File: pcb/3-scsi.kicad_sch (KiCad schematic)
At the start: 0 parts

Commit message: Phase 3: populate SCSI sheet and channel sheets
SCSI sheet (A2): IDC50 and HD50 wired by signal name from SCSI-2
Table 2, all four RESERVED lines grounded through 0R links, the
logic-analyzer header as a pin-for-pin copy of the Digital Discovery
DIN connector, three SN74LVTH245A terminators with their DIP-switch
enable and truth table, and one cluster per line: 2 x 220R terminator
pair, ESD diode and channel sheet. Channel sheets hold the FDV301N
driver and the 74LVC1G17 receiver; 18 instances, references page x 100.

Generator: repeated sheets, sheet symbols, native tables, and
deterministic UUIDs. Nets renamed: LA -> LOGIC_ANALYZER,
TERMINATOR_EN -> TERMINATOR_EN_INVERTED_FIRMWARE.
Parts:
- added C301, C302, C303: 100nF 50V, Capacitor_SMD:C_0402_1005Metric, symbol Device:C
- added D301, D302, D303, D304, D305, D306, D307, D308, D309, D310, D311, D312, D313, D314, D315, D316, D317, D318: H5VUD5BB, Diode_SMD:D_SOD-523, symbol Device:D_TVS
- added J301: IDC50 box header, Connector_IDC:IDC-Header_2x25_P2.54mm_Vertical, symbol Connector_Generic:Conn_02x25_Odd_Even
- added J302: HD50 female R/A, symbol Connector_Generic:Conn_02x25_Top_Bottom
- added J303: 2x16 box header, Connector_IDC:IDC-Header_2x16_P2.54mm_Vertical, symbol Connector_Generic:Conn_02x16_Odd_Even
- added R301, R302, R303, R304, R305, R306, R307, R308, R309, R310, R311, R312, R313, R314, R315, R316, R317, R318, R319, R320, R321, R322, R323, R324, R325, R326, R327, R328, R329, R330, R331, R332, R333, R334, R335, R336: 220R, Resistor_SMD:R_0402_1005Metric, symbol Device:R
- added R337, R338, R339, R340: 0R, Resistor_SMD:R_0402_1005Metric, symbol Device:R
- added R341: 10k, Resistor_SMD:R_0402_1005Metric, symbol Device:R
- added R342: 1k, Resistor_SMD:R_0402_1005Metric, symbol Device:R
- added SW301: DIP 2-pos, symbol Switch:SW_DIP_x02
- added U301, U302, U303: SN74LVTH245APWR, Package_SO:TSSOP-20_4.4x6.5mm_P0.65mm, symbol scsi-adapter:SN74LVTH245A
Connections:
- net ~{ACK}: now also D312.1 (A1), J301.38 (Pin_38), J302.44 (Pin_44), R323.2, R324.2
- net ~{ATN}: now also D310.1 (A1), J301.32 (Pin_32), J302.41 (Pin_41), R319.2, R320.2
- net ~{BSY}: now also D311.1 (A1), J301.36 (Pin_36), J302.43 (Pin_43), R321.2, R322.2
- net ~{CD}: now also D316.1 (A1), J301.46 (Pin_46), J302.48 (Pin_48), R331.2, R332.2
- net ~{DB0}: now also D301.1 (A1), J301.2 (Pin_2), J302.26 (Pin_26), R301.2, R302.2
- net ~{DB1}: now also D302.1 (A1), J301.4 (Pin_4), J302.27 (Pin_27), R303.2, R304.2
- net ~{DB2}: now also D303.1 (A1), J301.6 (Pin_6), J302.28 (Pin_28), R305.2, R306.2
- net ~{DB3}: now also D304.1 (A1), J301.8 (Pin_8), J302.29 (Pin_29), R307.2, R308.2
- net ~{DB4}: now also D305.1 (A1), J301.10 (Pin_10), J302.30 (Pin_30), R309.2, R310.2
- net ~{DB5}: now also D306.1 (A1), J301.12 (Pin_12), J302.31 (Pin_31), R311.2, R312.2
- net ~{DB6}: now also D307.1 (A1), J301.14 (Pin_14), J302.32 (Pin_32), R313.2, R314.2
- net ~{DB7}: now also D308.1 (A1), J301.16 (Pin_16), J302.33 (Pin_33), R315.2, R316.2
- net ~{DBP}: now also D309.1 (A1), J301.18 (Pin_18), J302.34 (Pin_34), R317.2, R318.2
- net ~{IO}: now also D318.1 (A1), J301.50 (Pin_50), J302.50 (Pin_50), R335.2, R336.2
- net ~{MSG}: now also D314.1 (A1), J301.42 (Pin_42), J302.46 (Pin_46), R327.2, R328.2
- net ~{REQ}: now also D317.1 (A1), J301.48 (Pin_48), J302.49 (Pin_49), R333.2, R334.2
- net ~{RST}: now also D313.1 (A1), J301.40 (Pin_40), J302.45 (Pin_45), R325.2, R326.2
- net ~{SEL}: now also D315.1 (A1), J301.44 (Pin_44), J302.47 (Pin_47), R329.2, R330.2
- new net: R342.1, SW301.4
- new net ACK_LOGIC_ANALYZER: J303.13 (Pin_13)
- new net ATN_LOGIC_ANALYZER: J303.17 (Pin_17)
- new net BSY_LOGIC_ANALYZER: J303.15 (Pin_15)
- new net CD_LOGIC_ANALYZER: J303.14 (Pin_14)
- new net DB0_LOGIC_ANALYZER: J303.29 (Pin_29)
- new net DB1_LOGIC_ANALYZER: J303.27 (Pin_27)
- new net DB2_LOGIC_ANALYZER: J303.25 (Pin_25)
- new net DB3_LOGIC_ANALYZER: J303.23 (Pin_23)
- new net DB4_LOGIC_ANALYZER: J303.30 (Pin_30)
- new net DB5_LOGIC_ANALYZER: J303.28 (Pin_28)
- new net DB6_LOGIC_ANALYZER: J303.26 (Pin_26)
- new net DB7_LOGIC_ANALYZER: J303.24 (Pin_24)
- new net DBP_LOGIC_ANALYZER: J303.19 (Pin_19)
- new net GND: C301.2, C302.2, C303.2, D301.2 (A2), D302.2 (A2), D303.2 (A2), D304.2 (A2), D305.2 (A2), D306.2 (A2), D307.2 (A2), D308.2 (A2), D309.2 (A2), D310.2 (A2), D311.2 (A2), D312.2 (A2), D313.2 (A2), D314.2 (A2), D315.2 (A2), D316.2 (A2), D317.2 (A2), D318.2 (A2), J301.1 (Pin_1), J301.11 (Pin_11), J301.13 (Pin_13), J301.15 (Pin_15), J301.17 (Pin_17), J301.19 (Pin_19), J301.20 (Pin_20), J301.21 (Pin_21), J301.22 (Pin_22), J301.29 (Pin_29), J301.3 (Pin_3), J301.30 (Pin_30), J301.31 (Pin_31), J301.33 (Pin_33), J301.34 (Pin_34), J301.35 (Pin_35), J301.37 (Pin_37), J301.39 (Pin_39), J301.41 (Pin_41), J301.43 (Pin_43), J301.45 (Pin_45), J301.47 (Pin_47), J301.49 (Pin_49), J301.5 (Pin_5), J301.7 (Pin_7), J301.9 (Pin_9), J302.1 (Pin_1), J302.10 (Pin_10), J302.11 (Pin_11), J302.15 (Pin_15), J302.16 (Pin_16), J302.17 (Pin_17), J302.18 (Pin_18), J302.19 (Pin_19), J302.2 (Pin_2), J302.20 (Pin_20), J302.21 (Pin_21), J302.22 (Pin_22), J302.23 (Pin_23), J302.24 (Pin_24), J302.25 (Pin_25), J302.3 (Pin_3), J302.35 (Pin_35), J302.36 (Pin_36), J302.4 (Pin_4), J302.40 (Pin_40), J302.42 (Pin_42), J302.5 (Pin_5), J302.6 (Pin_6), J302.7 (Pin_7), J302.8 (Pin_8), J302.9 (Pin_9), J303.1 (Pin_1), J303.11 (Pin_11), J303.12 (Pin_12), J303.2 (Pin_2), J303.21 (Pin_21), J303.22 (Pin_22), J303.31 (Pin_31), J303.32 (Pin_32), R337.2, R338.2, R339.2, R340.2, R342.2, U301.10 (GND), U302.10 (GND), U303.10 (GND)
- new net IO_LOGIC_ANALYZER: J303.7 (Pin_7)
- new net LOGIC_ANALYZER_MARKER0: J303.5 (Pin_5)
- new net LOGIC_ANALYZER_MARKER1: J303.3 (Pin_3)
- new net MSG_LOGIC_ANALYZER: J303.18 (Pin_18)
- new net REQ_LOGIC_ANALYZER: J303.9 (Pin_9)
- new net RST_LOGIC_ANALYZER: J303.20 (Pin_20)
- new net SCSI_RESERVED_23: J301.23 (Pin_23), J302.12 (Pin_12), R337.1
- new net SCSI_RESERVED_24: J301.24 (Pin_24), J302.37 (Pin_37), R338.1
- new net SCSI_RESERVED_27: J301.27 (Pin_27), J302.14 (Pin_14), R339.1
- new net SCSI_RESERVED_28: J301.28 (Pin_28), J302.39 (Pin_39), R340.1
- new net SEL_LOGIC_ANALYZER: J303.16 (Pin_16)
- new net TERMINATOR_EN_INVERTED: R341.2, SW301.1, SW301.2, U301.19 (CE), U302.19 (CE), U303.19 (CE)
- new net TERMINATOR_EN_INVERTED_FIRMWARE: SW301.3
- new net TERMINATOR_OUT_ACK: R323.1, R324.1, U302.13 (B5)
- new net TERMINATOR_OUT_ATN: R319.1, R320.1, U302.15 (B3)
- new net TERMINATOR_OUT_BSY: R321.1, R322.1, U302.14 (B4)
- new net TERMINATOR_OUT_CD: R331.1, R332.1, U303.15 (B3)
- new net TERMINATOR_OUT_DB0: R301.1, R302.1, U301.18 (B0)
- new net TERMINATOR_OUT_DB1: R303.1, R304.1, U301.17 (B1)
- new net TERMINATOR_OUT_DB2: R305.1, R306.1, U301.16 (B2)
- new net TERMINATOR_OUT_DB3: R307.1, R308.1, U301.15 (B3)
- new net TERMINATOR_OUT_DB4: R309.1, R310.1, U301.14 (B4)
- new net TERMINATOR_OUT_DB5: R311.1, R312.1, U301.13 (B5)
- new net TERMINATOR_OUT_DB6: R313.1, R314.1, U302.18 (B0)
- new net TERMINATOR_OUT_DB7: R315.1, R316.1, U302.17 (B1)
- new net TERMINATOR_OUT_DBP: R317.1, R318.1, U302.16 (B2)
- new net TERMINATOR_OUT_IO: R335.1, R336.1, U303.13 (B5)
- new net TERMINATOR_OUT_MSG: R327.1, R328.1, U303.17 (B1)
- new net TERMINATOR_OUT_REQ: R333.1, R334.1, U303.14 (B4)
- new net TERMINATOR_OUT_RST: R325.1, R326.1, U303.18 (B0)
- new net TERMINATOR_OUT_SEL: R329.1, R330.1, U303.16 (B2)
- new net TERMPWR: J301.26 (Pin_26), J302.38 (Pin_38)
- new net VTERMINATOR: C301.1, C302.1, C303.1, R341.1, U301.1 (A->B), U301.2 (A0), U301.20 (VCC), U301.3 (A1), U301.4 (A2), U301.5 (A3), U301.6 (A4), U301.7 (A5), U301.8 (A6), U301.9 (A7), U302.1 (A->B), U302.2 (A0), U302.20 (VCC), U302.3 (A1), U302.4 (A2), U302.5 (A3), U302.6 (A4), U302.7 (A5), U302.8 (A6), U302.9 (A7), U303.1 (A->B), U303.2 (A0), U303.20 (VCC), U303.3 (A1), U303.4 (A2), U303.5 (A3), U303.6 (A4), U303.7 (A5), U303.8 (A6), U303.9 (A7)
- no-connect marks 0 -> 12
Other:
- sheet ACK ports: added LOGIC_ANALYZER; removed LA
- sheet ATN ports: added LOGIC_ANALYZER; removed LA
- sheet BSY ports: added LOGIC_ANALYZER; removed LA
- sheet CD ports: added LOGIC_ANALYZER; removed LA
- sheet DB0 ports: added LOGIC_ANALYZER; removed LA
- sheet DB1 ports: added LOGIC_ANALYZER; removed LA
- sheet DB2 ports: added LOGIC_ANALYZER; removed LA
- sheet DB3 ports: added LOGIC_ANALYZER; removed LA
- sheet DB4 ports: added LOGIC_ANALYZER; removed LA
- sheet DB5 ports: added LOGIC_ANALYZER; removed LA
- sheet DB6 ports: added LOGIC_ANALYZER; removed LA
- sheet DB7 ports: added LOGIC_ANALYZER; removed LA
- sheet DBP ports: added LOGIC_ANALYZER; removed LA
- sheet IO ports: added LOGIC_ANALYZER; removed LA
- sheet MSG ports: added LOGIC_ANALYZER; removed LA
- sheet REQ ports: added LOGIC_ANALYZER; removed LA
- sheet RST ports: added LOGIC_ANALYZER; removed LA
- sheet SEL ports: added LOGIC_ANALYZER; removed LA
- note added: "A1-A8 and DIR tie straight to the rail: DIR high = A->B, and bus-hold inputs mustn't get pull resistors. B7/B8 unused."
- note added: "Active terminator"
- note added: "Connectors"
- note added: "J301 SCSI IDC50 (fitted)"
- note added: "J302 SCSI HD50 (DNP)"
- note added: "J303 logic-analyzer header (Digital Discovery DIN)"
- note added: "MSG, C/D, REQ, I/O: only the target drives them (SCSI-2 Table 6), so no driver."
- note added: "Per line: terminator pair (2 x 220R = 110R), ESD diode to GND, then the channel sheet (driver + receiver). Keep each cluster on its own bus trace by the connector. GATE (from the RP2350) and RX (to it) are sheet pins."
- note added: "Per-line driver and receiver"
- note added: "Pin 25 (HD50 13) is OPEN: a reversed ribbon puts TERMPWR on a dead pin, not on ground. IDC50 even pins 20, 22, 30, 34 are GROUND."
- note added: "Pin-for-pin copy of the Digital Discovery's 2x16 DIN connector (reference manual Fig. 8): a straight 32-way 0.1" IDC ribbon links pin n to pin n. DIN0-17 = the 18 bus lines in GPIO order (DB0..IO), DIN18/19 = the two markers, DIN20-23 unused. GND on 1, 2, 11, 12, 21, 22, 31, 32. Each tap has 100R at its receiver (channel sheets)."
- note added: "R301-R336: 220R 1 % 0402 (C25091), <= 35 mW each at 2.94 V into an asserted line. D301-D318: H5VUD5BB (C20615820), bidirectional, 0.3 pF, 5 V working. ESD protection: they clamp static discharges from the cable or a finger on the connector to GND before they reach the FET or the receiver. 0.3 pF keeps each line inside SCSI-2's 25 pF budget; bidirectional, so normal bus swings never make them cond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"
- note added: "Receive-only lines"
- note added: "SCSI-2 5.4.4: RESERVED lines 'shall be connected to ground' in end devices, 'should be open' otherwise. We are an end device: all four fitted. Remove R337-R340 if the board ever sits mid-chain."
- note added: "SCSI: the same bus on both, wired by signal name from SCSI-2 Table 2 (IDC50 = contact set 1, HD50 = set 2)."
- note added: "Switch state survives power-off and needs no firmware; DIP 2 lets firmware (expander P12) override it."
- note added: "TERMINATOR_EN_INVERTED drives /OE on U301-U303: low = terminated. R341 pulls it up to 2.83 V (off). DIP 1 closes it to GND through R342: ~0.26 V = on. DIP 2 connects it to the expander pin (push-pull, so it can override R342). The expander powers up with its pins as inputs, so the switch default holds; firmware reads the pin to learn it. Mid-chain and possibly unpowered: use off/off."
- note added: "Terminator enable DIP switch"
- note added: "VTERMINATOR (2.83 V) -> SN74LVTH245A, A tied high -> TERMINATOR_OUT_<line> -> 2 x 220R per line (next to each line, right) -> bus. /OE high or unpowered: outputs high-Z. 6 lines per package, in connector order."
- note removed: "SCSI front end (blocks/2-scsi-frontend.md, parts list §2) IDC50 + HD50 (DNP) connectors, 18 × H5VUD5BB ESD at the connector, RESERVED 0 Ω links, terminator: 3 × SN74LVTH245A + 36 × 220 Ω (2 per line) + DIP switch, LA header 2×16. Bus lines carry active-low (overbar) labels; channel sheets hold the per-line driver and receiver. ESD and terminators stay here so they can be placed at the connector."

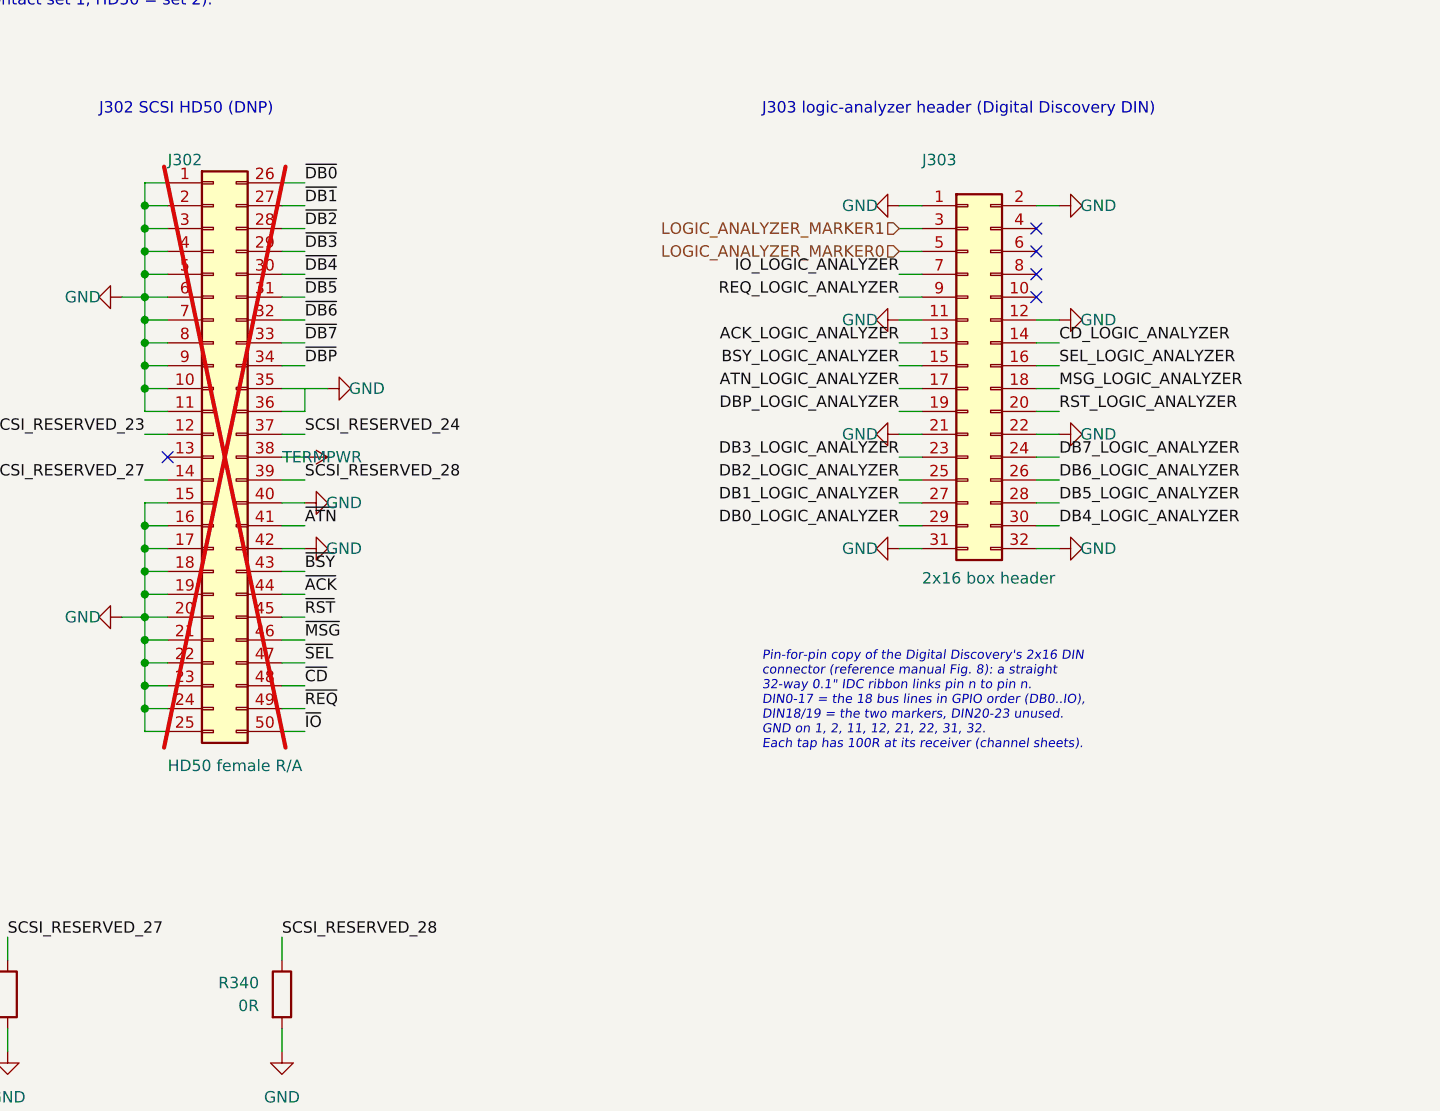
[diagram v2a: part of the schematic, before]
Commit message: Phase 3: footprint audit fixes and project footprint library
- New project footprint library pcb/scsi-adapter.pretty, generated by
  pcb/_gen/footprints.py from datasheet land patterns: TI RPW0010A (U101/U201),
  Kangnex WJ500V (J101), TE AMPLIMITE .050 HD50 (J302), SHOU HAN TF PUSH
  microSD (J501), Abracon AOTA-B201610 polarized inductor (L401), SHOU HAN
  2-pos DIP (SW301). fp-lib-table added.
- J303 LA header: 2x17 box header C20920, pins 33/34 NC (34-way ribbon to a
  future 2x16 adapter board).
- J302 HD50: TE 5787082-5 squeeze-latch receptacle; shielded symbol, shell to
  GND via R343 0R. TE STEP model git-ignored (pcb/scsi-adapter.3dshapes/).
- D101/D204/D605: D_SMF -> D_SOD-123F (parts are SOD-123FL).
- L401 pins swapped so pad 1 = polarity dot = DVDD_1V1 (RP2350 Fig. 23).
- SW401/SW402: Hroparts K2-1102DP C110153 on SW_PUSH_6mm.
- NOTES, decisions, sources updated; J601 pad question closed; RP2350B
  minimal-design layout copy planned (open question 17).
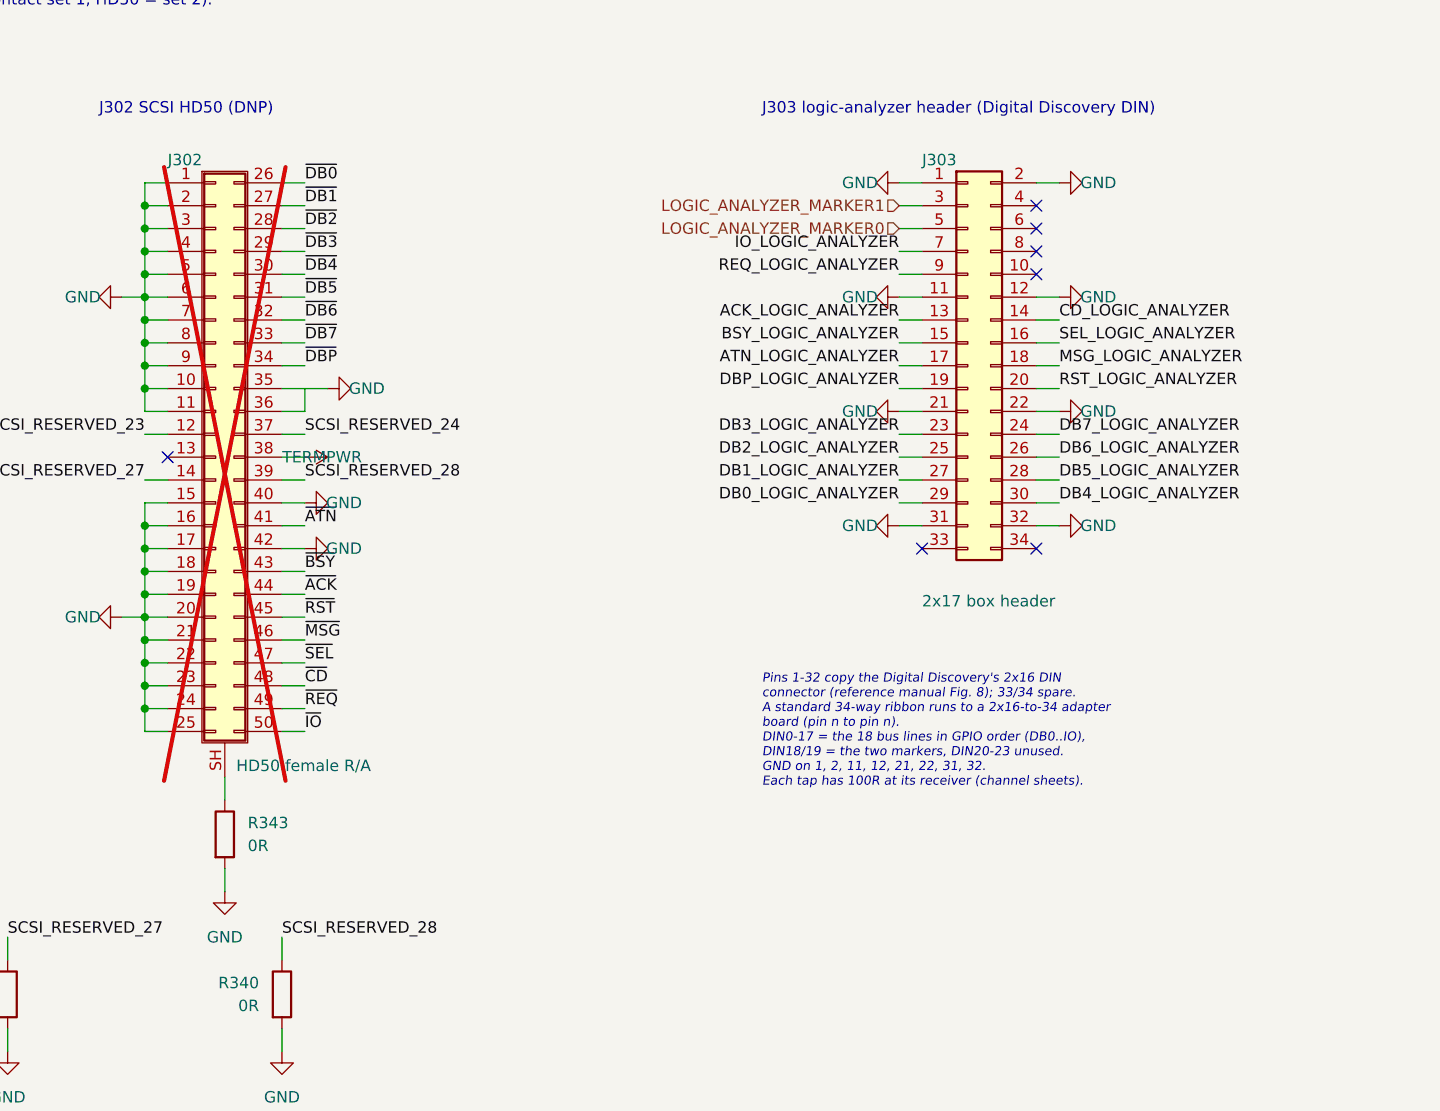
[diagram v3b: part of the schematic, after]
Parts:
- removed J303: 2x16 box header, Connector_IDC:IDC-Header_2x16_P2.54mm_Vertical, symbol Connector_Generic:Conn_02x16_Odd_Even
- removed R337: 0R, Resistor_SMD:R_0402_1005Metric, symbol Device:R
- added J303: 2x17 box header, Connector_IDC:IDC-Header_2x17_P2.54mm_Vertical, symbol Connector_Generic:Conn_02x17_Odd_Even
- added R340, R343: 0R, Resistor_SMD:R_0402_1005Metric, symbol Device:R
- J302: footprint (none) -> scsi-adapter:TE_AMPLIMITE-050_5787082-5_50pos_P1.27mm_Horizontal; symbol Connector_Generic:Conn_02x25_Top_Bottom -> Connector_Generic_Shielded:Conn_02x25_Top_Bottom_Shielded
- SW301: footprint (none) -> scsi-adapter:SW_DIP_SPSTx02_Slide_SHOUHAN_2.54-2P-TPGT_W8.8mm_P2.54mm
- renumbered R338 to R337, R339 to R338, R340 to R339
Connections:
- net ACK_LOGIC_ANALYZER: now also J303.13 (Pin_13)
- net ATN_LOGIC_ANALYZER: now also J303.17 (Pin_17)
- net BSY_LOGIC_ANALYZER: now also J303.15 (Pin_15)
- net CD_LOGIC_ANALYZER: now also J303.14 (Pin_14)
- net DB0_LOGIC_ANALYZER: now also J303.29 (Pin_29)
- net DB1_LOGIC_ANALYZER: now also J303.27 (Pin_27)
- net DB2_LOGIC_ANALYZER: now also J303.25 (Pin_25)
- net DB3_LOGIC_ANALYZER: now also J303.23 (Pin_23)
- net DB4_LOGIC_ANALYZER: now also J303.30 (Pin_30)
- net DB5_LOGIC_ANALYZER: now also J303.28 (Pin_28)
- net DB6_LOGIC_ANALYZER: now also J303.26 (Pin_26)
- net DB7_LOGIC_ANALYZER: now also J303.24 (Pin_24)
- net DBP_LOGIC_ANALYZER: now also J303.19 (Pin_19)
- net GND: now also J303.1 (Pin_1), J303.11 (Pin_11), J303.12 (Pin_12), J303.2 (Pin_2), J303.21 (Pin_21), J303.22 (Pin_22), J303.31 (Pin_31), J303.32 (Pin_32), R340.2, R343.2
- net IO_LOGIC_ANALYZER: now also J303.7 (Pin_7)
- net LOGIC_ANALYZER_MARKER0: now also J303.5 (Pin_5)
- net LOGIC_ANALYZER_MARKER1: now also J303.3 (Pin_3)
- net MSG_LOGIC_ANALYZER: now also J303.18 (Pin_18)
- net REQ_LOGIC_ANALYZER: now also J303.9 (Pin_9)
- net RST_LOGIC_ANALYZER: now also J303.20 (Pin_20)
- net SCSI_RESERVED_23: now also R337.1
- net SCSI_RESERVED_24: now also R338.1; no longer R337.1
- net SCSI_RESERVED_27: now also R339.1; no longer R338.1
- net SCSI_RESERVED_28: now also R340.1; no longer R339.1
- net SEL_LOGIC_ANALYZER: now also J303.16 (Pin_16)
- new net: J302.SH (Shield), R343.1
- no-connect marks 12 -> 14
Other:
- note added: "Pins 1-32 copy the Digital Discovery's 2x16 DIN connector (reference manual Fig. 8); 33/34 spare. A standard 34-way ribbon runs to a 2x16-to-34 adapter board (pin n to pin n). DIN0-17 = the 18 bus lines in GPIO order (DB0..IO), DIN18/19 = the two markers, DIN20-23 unused. GND on 1, 2, 11, 12, 21, 22, 31, 32. Each tap has 100R at its receiver (channel sheets)."
- note removed: "Pin-for-pin copy of the Digital Discovery's 2x16 DIN connector (reference manual Fig. 8): a straight 32-way 0.1" IDC ribbon links pin n to pin n. DIN0-17 = the 18 bus lines in GPIO order (DB0..IO), DIN18/19 = the two markers, DIN20-23 unused. GND on 1, 2, 11, 12, 21, 22, 31, 32. Each tap has 100R at its receiver (channel sheets)."
- moved on the sheet: R337, R338, R339

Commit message: route more scsi traces
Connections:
- net TERMINATOR_OUT_ACK: now also U302.16 (B2); no longer U302.13 (B5)
- net TERMINATOR_OUT_ATN: now also U302.18 (B0); no longer U302.15 (B3)
- net TERMINATOR_OUT_BSY: now also U302.17 (B1); no longer U302.14 (B4)
- net TERMINATOR_OUT_DB0: now also U301.15 (B3); no longer U301.18 (B0)
- net TERMINATOR_OUT_DB1: now also U301.14 (B4); no longer U301.17 (B1)
- net TERMINATOR_OUT_DB2: now also U301.13 (B5); no longer U301.16 (B2)
- net TERMINATOR_OUT_DB3: now also U301.18 (B0); no longer U301.15 (B3)
- net TERMINATOR_OUT_DB4: now also U301.17 (B1); no longer U301.14 (B4)
- net TERMINATOR_OUT_DB5: now also U301.16 (B2); no longer U301.13 (B5)
- net TERMINATOR_OUT_DB6: now also U302.15 (B3); no longer U302.18 (B0)
- net TERMINATOR_OUT_DB7: now also U302.14 (B4); no longer U302.17 (B1)
- net TERMINATOR_OUT_DBP: now also U302.13 (B5); no longer U302.16 (B2)

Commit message: route logic analyzer and bus crystal
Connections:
- net ACK_LOGIC_ANALYZER: now also J303.19 (Pin_19); no longer J303.13 (Pin_13)
- net ATN_LOGIC_ANALYZER: now also J303.23 (Pin_23); no longer J303.17 (Pin_17)
- net BSY_LOGIC_ANALYZER: now also J303.24 (Pin_24); no longer J303.15 (Pin_15)
- net CD_LOGIC_ANALYZER: now also J303.29 (Pin_29); no longer J303.14 (Pin_14)
- net DB0_LOGIC_ANALYZER: now also J303.14 (Pin_14); no longer J303.29 (Pin_29)
- net DB1_LOGIC_ANALYZER: now also J303.9 (Pin_9); no longer J303.27 (Pin_27)
- net DB2_LOGIC_ANALYZER: now also J303.7 (Pin_7); no longer J303.25 (Pin_25)
- net DB3_LOGIC_ANALYZER: now also J303.15 (Pin_15); no longer J303.23 (Pin_23)
- net DB4_LOGIC_ANALYZER: now also J303.16 (Pin_16); no longer J303.30 (Pin_30)
- net DB5_LOGIC_ANALYZER: now also J303.13 (Pin_13); no longer J303.28 (Pin_28)
- net DB6_LOGIC_ANALYZER: now also J303.20 (Pin_20); no longer J303.26 (Pin_26)
- net DB7_LOGIC_ANALYZER: now also J303.17 (Pin_17); no longer J303.24 (Pin_24)
- net DBP_LOGIC_ANALYZER: now also J303.18 (Pin_18); no longer J303.19 (Pin_19)
- net IO_LOGIC_ANALYZER: now also J303.27 (Pin_27); no longer J303.7 (Pin_7)
- net MSG_LOGIC_ANALYZER: now also J303.25 (Pin_25); no longer J303.18 (Pin_18)
- net REQ_LOGIC_ANALYZER: now also J303.30 (Pin_30); no longer J303.9 (Pin_9)
- net RST_LOGIC_ANALYZER: now also J303.28 (Pin_28); no longer J303.20 (Pin_20)
- net SEL_LOGIC_ANALYZER: now also J303.26 (Pin_26); no longer J303.16 (Pin_16)
- net TERMINATOR_OUT_CD: now also U303.18 (B0); no longer U303.15 (B3)
- net TERMINATOR_OUT_IO: now also U303.16 (B2); no longer U303.13 (B5)
- net TERMINATOR_OUT_MSG: now also U303.14 (B4); no longer U303.17 (B1)
- net TERMINATOR_OUT_REQ: now also U303.17 (B1); no longer U303.14 (B4)
- net TERMINATOR_OUT_RST: now also U303.15 (B3); no longer U303.18 (B0)
- net TERMINATOR_OUT_SEL: now also U303.13 (B5); no longer U303.16 (B2)
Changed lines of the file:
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@@
 		)
 	)
-	(label "DB3_LOGIC_ANALYZER"
+	(label "ATN_LOGIC_ANALYZER"
 		(at 193.04 73.66 180)
 		(effects
@@
 		)
 	)
-	(label "BSY_LOGIC_ANALYZER"
+	(label "DB3_LOGIC_ANALYZER"
 		(at 193.04 63.5 180)
 		(effects
@@
 		)
 	)
-	(label "TERMINATOR_OUT_REQ"
+	(label "TERMINATOR_OUT_MSG"
 		(at 231.14 231.14 0)
 		(effects
@@
 		)
 	)
-	(label "DB7_LOGIC_ANALYZER"
+	(label "BSY_LOGIC_ANALYZER"
 		(at 210.82 73.66 0)
 		(effects
@@
 		)
 	)
-	(label "TERMINATOR_OUT_CD"
+	(label "TERMINATOR_OUT_RST"
 		(at 231.14 228.6 0)
 		(effects
@@
 		)
 	)
-	(label "DB0_LOGIC_ANALYZER"
+	(label "CD_LOGIC_ANALYZER"
 		(at 193.04 81.28 180)
 		(effects
@@
 		)
 	)
-	(label "SEL_LOGIC_ANALYZER"
+	(label "DB4_LOGIC_ANALYZER"
 		(at 210.82 63.5 0)
 		(effects
@@
 		)
 	)
-	(label "DB5_LOGIC_ANALYZER"
+	(label "RST_LOGIC_ANALYZER"
 		(at 210.82 78.74 0)
 		(effects
@@
 		)
 	)
-	(label "MSG_LOGIC_ANALYZER"
+	(label "DBP_LOGIC_ANALYZER"
 		(at 210.82 66.04 0)
 		(effects
@@
 		)
 	)
-	(label "TERMINATOR_OUT_MSG"
+	(label "TERMINATOR_OUT_REQ"
 		(at 231.14 223.52 0)
 		(effects
@@
 		)
 	)
-	(label "DBP_LOGIC_ANALYZER"
+	(label "ACK_LOGIC_ANALYZER"
 		(at 193.04 68.58 180)
 		(effects
@@
 		)
 	)
-	(label "TERMINATOR_OUT_IO"
+	(label "TERMINATOR_OUT_SEL"
 		(at 231.14 233.68 0)
 		(effects
@@
 		)
 	)
-	(label "REQ_LOGIC_ANALYZER"
+	(label "DB1_LOGIC_ANALYZER"
 		(at 193.04 55.88 180)
 		(effects
@@
 		)
 	)
-	(label "DB4_LOGIC_ANALYZER"
+	(label "REQ_LOGIC_ANALYZER"
 		(at 210.82 81.28 0)
 		(effects
@@
 		)
 	)
-	(label "ACK_LOGIC_ANALYZER"
+	(label "DB5_LOGIC_ANALYZER"
 		(at 193.04 60.96 180)
 		(effects
@@
 		)
 	)
-	(label "ATN_LOGIC_ANALYZER"
+	(label "DB7_LOGIC_ANALYZER"
 		(at 193.04 66.04 180)
 		(effects
@@
 		)
 	)
-	(label "IO_LOGIC_ANALYZER"
+	(label "DB2_LOGIC_ANALYZER"
 		(at 193.04 53.34 180)
 		(effects
@@
 		)
 	)
-	(label "TERMINATOR_OUT_RST"
+	(label "TERMINATOR_OUT_CD"
 		(at 231.14 220.98 0)
 		(effects
@@
 		)
 	)
-	(label "TERMINATOR_OUT_SEL"
+	(label "TERMINATOR_OUT_IO"
 		(at 231.14 226.06 0)
 		(effects
@@
 		)
 	)
-	(label "DB2_LOGIC_ANALYZER"
+	(label "MSG_LOGIC_ANALYZER"
 		(at 193.04 76.2 180)
 		(effects
@@
 		)
 	)
-	(label "DB6_LOGIC_ANALYZER"
+	(label "SEL_LOGIC_ANALYZER"
 		(at 210.82 76.2 0)
 		(effects
@@
 		)
 	)
-	(label "CD_LOGIC_ANALYZER"
+	(label "DB0_LOGIC_ANALYZER"
 		(at 210.82 60.96 0)
 		(effects
@@
 		)
 	)
-	(label "DB1_LOGIC_ANALYZER"
+	(label "IO_LOGIC_ANALYZER"
 		(at 193.04 78.74 180)
 		(effects
@@
 		)
 	)
-	(label "RST_LOGIC_ANALYZER"
+	(label "DB6_LOGIC_ANALYZER"
 		(at 210.82 68.58 0)
 		(effects
